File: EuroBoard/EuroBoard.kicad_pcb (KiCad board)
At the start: 2 copper layers, 100 x 100 mm, 21 parts, among them J1 SPI, SW1 RESET, SW2 BOOT, U1 AMS1117-3.3, U2 STM32G030CxT, Y1 NX2520 16MHz

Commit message: Started doing PCB
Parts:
- removed R3: R, Resistor_SMD:R_0805_2012Metric_Pad1.20x1.40mm_HandSolder
- removed SW2: BOOT, Button_Switch_SMD:SW_SPST_B3U-1000P-B
- added C10: 100n, Capacitor_SMD:C_0805_2012Metric_Pad1.18x1.45mm_HandSolder, F.Cu at (146.1, 48.3)
- added C11: 10u, Capacitor_SMD:C_0805_2012Metric_Pad1.18x1.45mm_HandSolder, F.Cu at (146.1, 50.8)
- added C9: 10u, Capacitor_SMD:C_0805_2012Metric_Pad1.18x1.45mm_HandSolder, F.Cu at (153.7, 50.8)
- added D2: 1n4148, Diode_SMD:D_SOD-123, F.Cu at (156.1, 79.2)
- added J2: I2C, Connector_PinSocket_2.54mm:PinSocket_1x03_P2.54mm_Vertical, F.Cu at (101.6, 78.7)
- added J3: UART, Connector_PinSocket_2.54mm:PinSocket_1x03_P2.54mm_Vertical, F.Cu at (101.6, 55.9)
- C3, C8: moved to B.Cu
- C4: value 4.7u -> 10u; moved to B.Cu
- SW1: footprint Button_Switch_SMD:SW_SPST_B3U-1000P-B -> Button_Switch_SMD:SW_SPST_B3S-1000
- moved C8 75.2 mm to (146.3, 64.0), turned to 180 degrees
- moved F1 72.9 mm to (156.5, 50.7), turned to 90 degrees
- moved C5 72.2 mm to (152.2, 45.7)
- moved U2 71.5 mm to (151.3, 63.9), turned to 45 degrees
- moved C4 68.6 mm to (151.4, 66.0)
- moved C3 68.2 mm to (151.4, 64.0)
- moved L1 66.9 mm to (147.1, 44.7), turned to -90 degrees
- moved C1 62.5 mm to (142.2, 67.9), turned to 180 degrees
- moved SW1 60.1 mm to (92.0, 41.0)
- moved U1 56.5 mm to (154.3, 40.6), turned to 0 degrees
- moved C6 55.0 mm to (148.2, 39.4), turned to 90 degrees
- moved C2 55.0 mm to (142.2, 74.7), turned to 180 degrees
- moved D1 53.6 mm to (142.2, 62.0), turned to 180 degrees
- moved C7 53.2 mm to (139.1, 71.1), turned to 90 degrees
- moved R1 52.9 mm to (145.2, 71.1), turned to 90 degrees
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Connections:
- net Net-(R2-Pad2) renamed /LED
- C2 pad 1: /RST -> Net-(C2-Pad1)
- C6 pad 1: +3.3V -> Net-(L1-Pad1)
- C8 pad 1: +3.3V -> /VREF
- F1 pad 2: Net-(F1-Pad2) -> Net-(C5-Pad1)
- L1 pad 1: Net-(F1-Pad2) -> Net-(L1-Pad1)
- L1 pad 2: Net-(C5-Pad1) -> +3.3V
- SW1 pad 2: /RST -> Net-(C2-Pad1)
- U1 pad 2: +3.3V -> Net-(L1-Pad1)
- U2 pad 10: /RST -> Net-(C2-Pad1)
- U2 pad 29: /SCL -> /TX_AUX
- U2 pad 32: /SDA -> /RX_AUX
- U2 pad 45: unconnected-(U2-Pad45) -> /SCL
- U2 pad 46: unconnected-(U2-Pad46) -> /SDA
- U2 pad 5: +3.3V -> /VREF
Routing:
- net /SCL: track 0.00 -> 32.2 mm
- net +3.3V: track 0.00 -> 30.8 mm, vias 0 -> 2
- net GND: track 0.00 -> 30.6 mm, vias 0 -> 1
- net Net-(L1-Pad1): track 0.00 -> 13.4 mm
- net Net-(C5-Pad1): track 0.00 -> 11.5 mm
- net Net-(C2-Pad1): track 0.00 -> 10.7 mm
- net /OSC_IN: track 0.00 -> 8.60 mm
- net +5V: track 0.00 -> 7.74 mm
- net Net-(C7-Pad1): track 0.00 -> 6.98 mm
- net /VREF: track 0.00 -> 5.62 mm, vias 0 -> 1
- net /OSC_OUT: track 0.00 -> 5.04 mm
- net /LED: track 0.00 -> 4.14 mm
- net -12V: track 0.00 -> 2.54 mm
- net +12V: track 0.00 -> 2.54 mm
- net Net-(D1-Pad2): track 0.00 -> 2.05 mm

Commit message: Board outline
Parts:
- added C12: 10u, Capacitor_SMD:C_0805_2012Metric_Pad1.18x1.45mm_HandSolder, B.Cu at (131.1, 38.1)
- added C13: 10u, Capacitor_SMD:C_0805_2012Metric_Pad1.18x1.45mm_HandSolder, B.Cu at (131.1, 40.6)
- added C14: 10u, Capacitor_SMD:C_0805_2012Metric_Pad1.18x1.45mm_HandSolder, B.Cu at (131.1, 43.2)
- added C15: 10u, Capacitor_SMD:C_0805_2012Metric_Pad1.18x1.45mm_HandSolder, B.Cu at (131.1, 45.7)
- added J4: Conn_01x05_Male, Connector_PinHeader_2.54mm:PinHeader_1x05_P2.54mm_Vertical, F.Cu at (134.6, 38.1)
- added SW2: SW_DIP_x04, Button_Switch_SMD:SW_DIP_SPSTx04_Slide_Omron_A6H-4101_W6.15mm_P1.27mm, F.Cu at (155.0, 61.0)
- C4: value 10u -> 4.7u; moved to F.Cu
- J1: value SPI -> GPIO; footprint Connector_PinHeader_2.54mm:PinHeader_1x04_P2.54mm_Vertical -> Connector_PinHeader_2.54mm:PinHeader_1x08_P2.54mm_Vertical
- J2: value I2C -> Conn_01x07_Male; footprint Connector_PinSocket_2.54mm:PinSocket_1x03_P2.54mm_Vertical -> Connector_PinHeader_2.54mm:PinHeader_1x07_P2.54mm_Vertical
- J3: value UART -> I2C; footprint Connector_PinSocket_2.54mm:PinSocket_1x03_P2.54mm_Vertical -> Connector_PinHeader_2.54mm:PinHeader_1x03_P2.54mm_Vertical
- moved J3 57.0 mm to (156.0, 73.0)
- moved SW1 50.5 mm to (142.5, 40.2)
- moved J2 48.0 mm to (127.0, 38.0), turned to 0 degrees
- moved J1 25.9 mm to (127.0, 63.5), turned to 0 degrees
- moved R2 17.9 mm to (144.3, 46.2)
- moved C4 17.9 mm to (133.9, 62.5), turned to 135 degrees
- moved C10 16.2 mm to (135.6, 60.7), turned to 135 degrees
- moved D1 15.9 mm to (140.2, 46.2), turned to 0 degrees
- moved C9 14.9 mm to (160.5, 37.5), turned to 0 degrees
- moved D2 14.2 mm to (143.3, 73.2), turned to 45 degrees
- moved F1 10.5 mm to (160.5, 41.0), turned to 180 degrees
- moved C3 8.91 mm to (142.5, 63.8)
- moved C6 8.05 mm to (151.5, 46.7), turned to 180 degrees
- moved U2 7.64 mm to (144.2, 61.1)
- moved C1 7.18 mm to (135.4, 65.5), turned to -135 degrees
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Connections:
- J1 pad 1: /SPI1_SCK -> Net-(J1-Pad1)
- J1 pad 2: /SPI1_MISO -> /SPI1_SCK
- J1 pad 3: /SPI1_MISO -> /TX_DEBUG
- J1 pad 4: GND -> /RX_DEBUG
- J2 pad 1: /SCL2 -> Net-(J2-Pad1)
- J2 pad 2: /SDA2 -> Net-(J2-Pad2)
- J2 pad 3: GND -> Net-(J2-Pad3)
- J3 pad 1: /TX_AUX -> /SCL2
- J3 pad 2: /RX_AUX -> /SDA2
- U2 pad 11: unconnected-(U2-Pad11) -> Net-(J1-Pad1)
- U2 pad 15: unconnected-(U2-Pad15) -> Net-(J1-Pad5)
- U2 pad 16: unconnected-(U2-Pad16) -> Net-(J1-Pad6)
- U2 pad 24: unconnected-(U2-Pad24) -> Net-(U2-Pad24)
- U2 pad 25: unconnected-(U2-Pad25) -> Net-(U2-Pad25)
- U2 pad 26: unconnected-(U2-Pad26) -> Net-(U2-Pad26)
- U2 pad 27: unconnected-(U2-Pad27) -> Net-(U2-Pad27)
- U2 pad 42: unconnected-(U2-Pad42) -> Net-(J2-Pad1)
- U2 pad 43: unconnected-(U2-Pad43) -> Net-(J2-Pad2)
- U2 pad 44: unconnected-(U2-Pad44) -> Net-(J2-Pad3)
- U2 pad 47: unconnected-(U2-Pad47) -> Net-(J2-Pad6)
- U2 pad 48: unconnected-(U2-Pad48) -> Net-(J2-Pad7)
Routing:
- net +3.3V: track 30.8 -> 132.9 mm
- net /TX_DEBUG: track 0.00 -> 80.4 mm, vias 0 -> 1
- net /RX_DEBUG: track 0.00 -> 75.5 mm, vias 0 -> 1
- net /SWCLK: track 0.00 -> 65.9 mm
- net /SWDIO: track 0.00 -> 62.6 mm, vias 0 -> 1
- net /RST: track 0.00 -> 57.4 mm, vias 0 -> 1
- net /SDA: track 0.00 -> 51.3 mm, vias 0 -> 1
- net +5V: track 7.74 -> 55.1 mm
- net /SPI1_MOSI: track 0.00 -> 45.2 mm, vias 0 -> 1
- net /SPI1_MISO: track 0.00 -> 41.6 mm, vias 0 -> 1
- net Net-(C2-Pad1): track 10.7 -> 49.4 mm, vias 0 -> 2
- net Net-(J1-Pad6): track 0.00 -> 37.9 mm, vias 0 -> 1
- net +12V: track 2.54 -> 39.0 mm
- net Net-(J1-Pad5): track 0.00 -> 33.8 mm, vias 0 -> 1
- net -12V: track 2.54 -> 36.0 mm
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- added copper zone on B.Cu, net GND
- added copper zone on F.Cu, net GND

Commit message: Board awaiting review
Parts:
- removed C10, C3: 100n, Capacitor_SMD:C_0805_2012Metric_Pad1.18x1.45mm_HandSolder
- added J10: PD1, TestPoint:TestPoint_Pad_1.0x1.0mm, F.Cu at (143.3, 50.5)
- added J11: PD2, TestPoint:TestPoint_Pad_1.0x1.0mm, F.Cu at (141.0, 50.5)
- added J12: PD3, TestPoint:TestPoint_Pad_1.0x1.0mm, F.Cu at (138.7, 50.5)
- added J5: RX, TestPoint:TestPoint_Pad_1.0x1.0mm, F.Cu at (148.5, 55.4)
- added J6: TX, TestPoint:TestPoint_Pad_1.0x1.0mm, F.Cu at (150.0, 56.9)
- added J7: GND, TestPoint:TestPoint_Pad_1.0x1.0mm, F.Cu at (145.3, 50.5)
- added REF**: ProtoArea, MEMS_Custom:ProtoArea, F.Cu at (78.0, 37.0)
- L1: footprint Inductor_SMD:L_0805_2012Metric -> Inductor_SMD:L_0805_2012Metric_Pad1.15x1.40mm_HandSolder
- moved SW2 4.13 mm to (155.4, 56.9), turned to 90 degrees
- moved J3 2.93 mm to (156.5, 70.1)
- moved C4 1.21 mm to (133.6, 63.7), turned to -135 degrees
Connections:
- U2 pad 19: unconnected-(U2-Pad19) -> /TRG
- U2 pad 20: unconnected-(U2-Pad20) -> /RDY
- U2 pad 39: unconnected-(U2-Pad39) -> Net-(U2-Pad39)
- U2 pad 40: unconnected-(U2-Pad40) -> Net-(U2-Pad40)
- U2 pad 41: unconnected-(U2-Pad41) -> Net-(U2-Pad41)
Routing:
- net /RDY: track 0.00 -> 38.3 mm, vias 0 -> 1
- net /TRG: track 0.00 -> 36.7 mm, vias 0 -> 1
- net +3.3V: track 132.9 -> 145.6 mm
- net +5V: track 55.1 -> 67.5 mm, vias 0 -> 1
- net /SWDIO: track 62.6 -> 73.9 mm
- net /SWCLK: track 65.9 -> 75.9 mm
- net /SCL: track 50.1 -> 59.6 mm
- net Net-(U2-Pad41): track 0.00 -> 8.37 mm
- net /RX_DEBUG: track 75.5 -> 83.6 mm
- net Net-(SW2-Pad4): track 3.14 -> 11.2 mm
- net /TX_DEBUG: track 80.4 -> 88.2 mm
- net Net-(U2-Pad40): track 0.00 -> 7.64 mm
- net Net-(U2-Pad39): track 0.00 -> 7.33 mm
- net /SDA: track 51.3 -> 58.4 mm
- net -12V: track 36.0 -> 42.8 mm
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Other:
- board text added: "-12V"
- board text added: "12V"
- board text added: "3.3V"
- board text added: "5V"
- board text added: "EuroMeasure Evaluation Module v1.0"
- board text added: "GND"
- board text added: "Michał Zychla 2023"
- board text added: "SCL"
- board text added: "SDA"

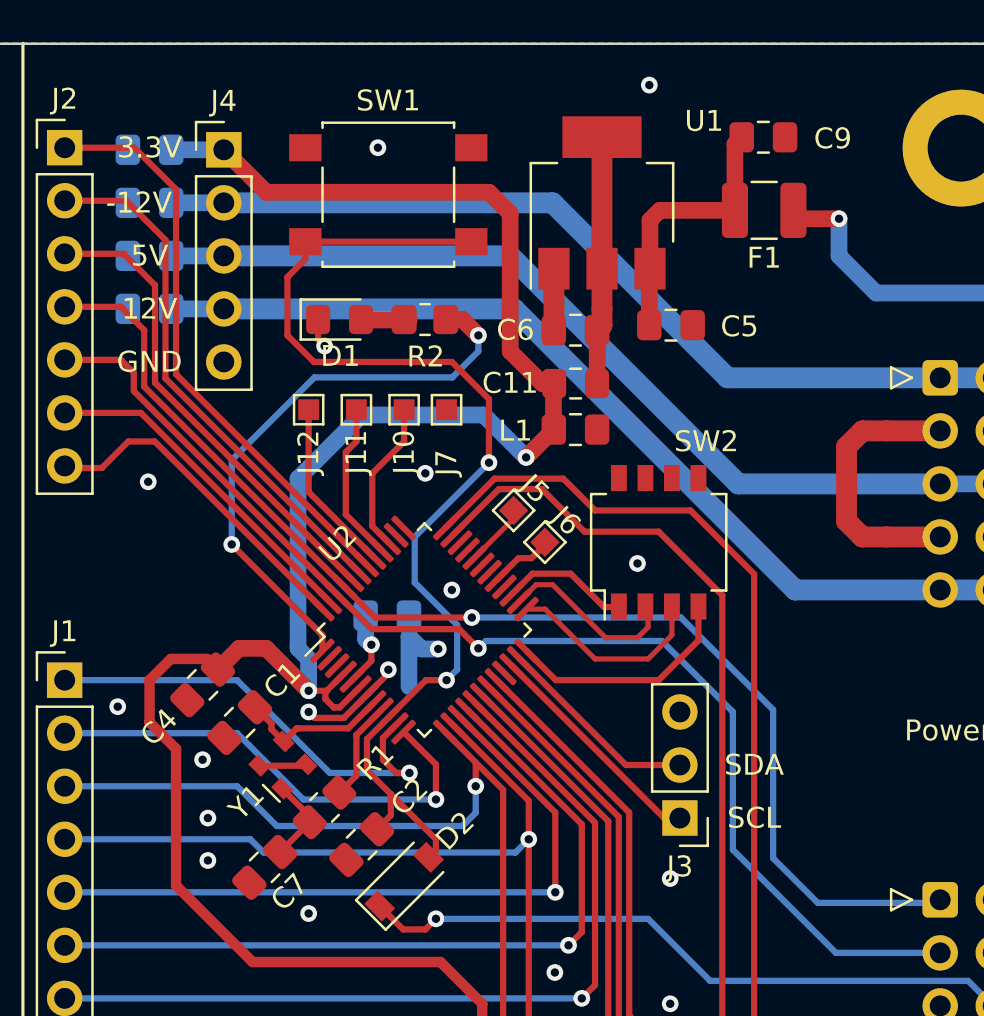
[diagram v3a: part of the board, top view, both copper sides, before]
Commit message: Removed unnecessary caps
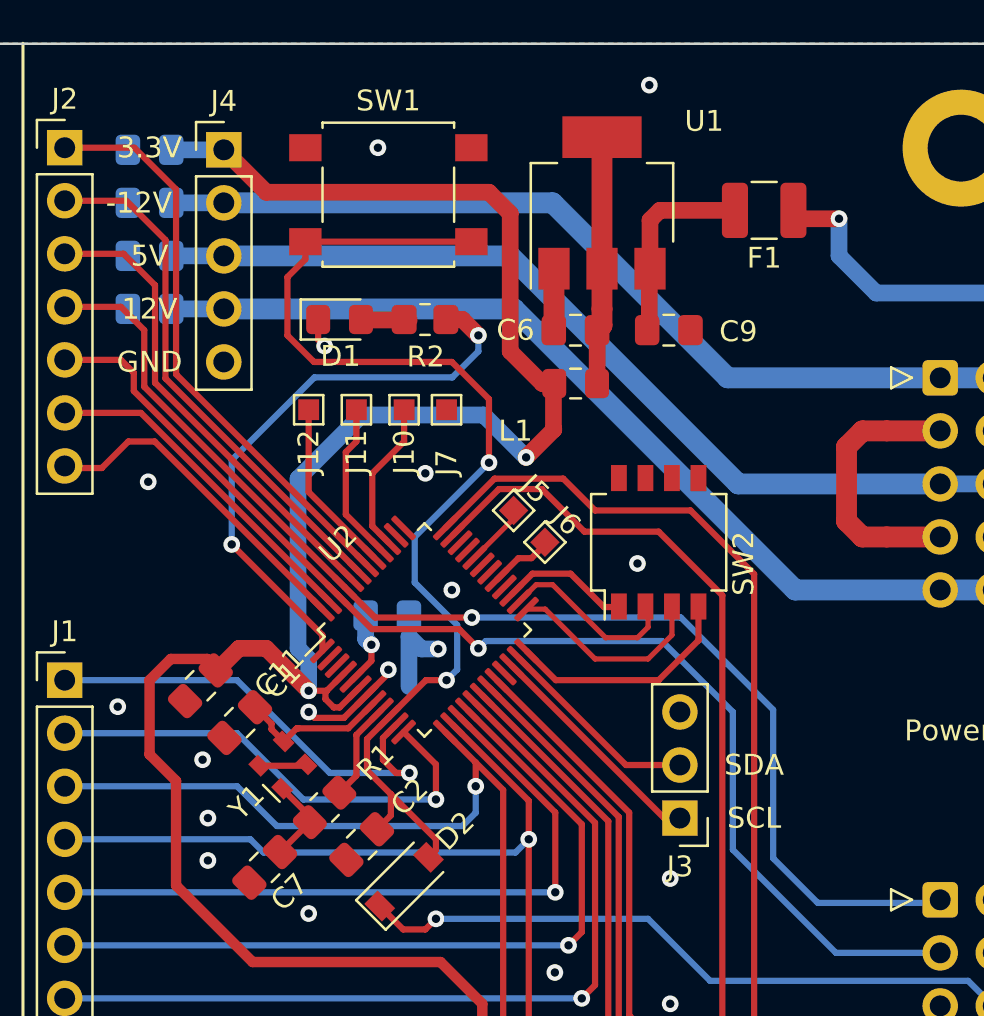
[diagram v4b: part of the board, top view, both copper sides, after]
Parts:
- removed C4: 4.7u, Capacitor_SMD:C_0805_2012Metric_Pad1.18x1.45mm_HandSolder
- removed C5: 1u, Capacitor_SMD:C_0805_2012Metric_Pad1.18x1.45mm_HandSolder
- moved C11 21.8 mm to (133.5, 63.8), turned to -135 degrees
- moved C9 10.3 mm to (155.9, 46.7)
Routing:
- net Net-(C5-Pad1): track 12.9 -> 9.31 mm

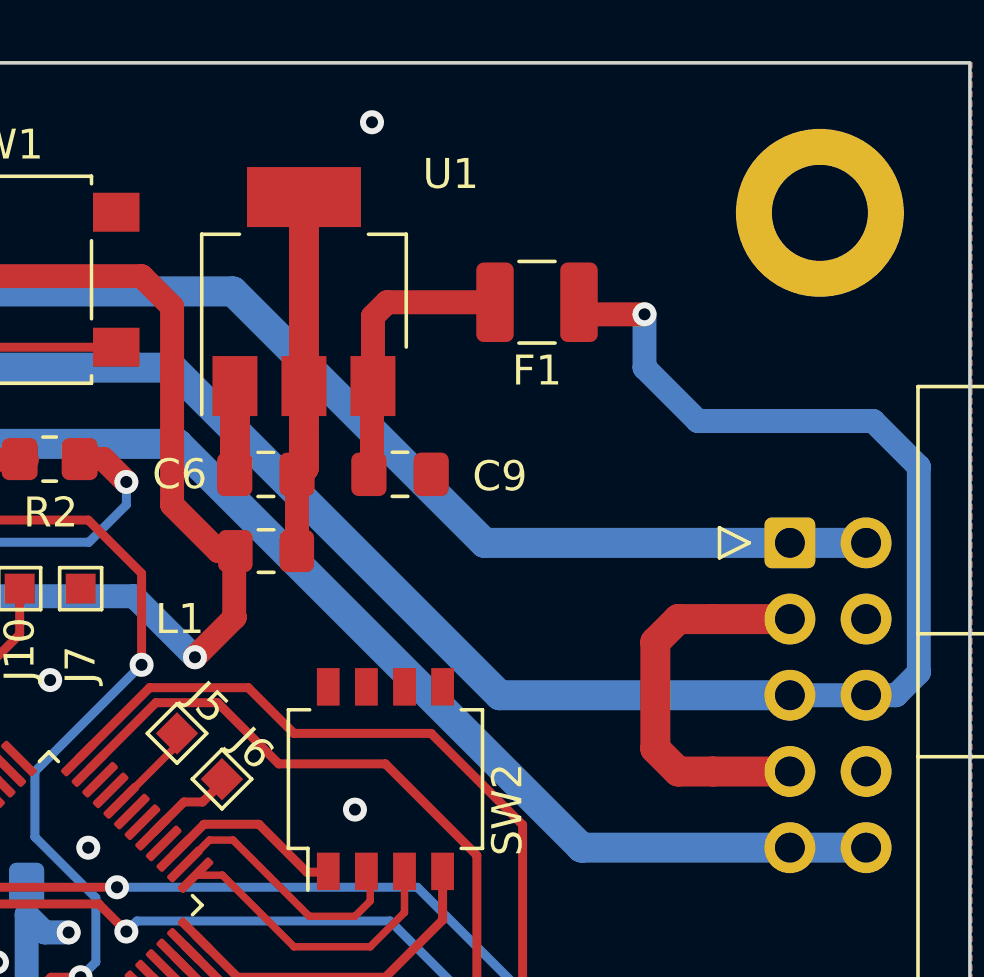
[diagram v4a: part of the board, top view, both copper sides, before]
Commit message: Added alectrolytic capacitors
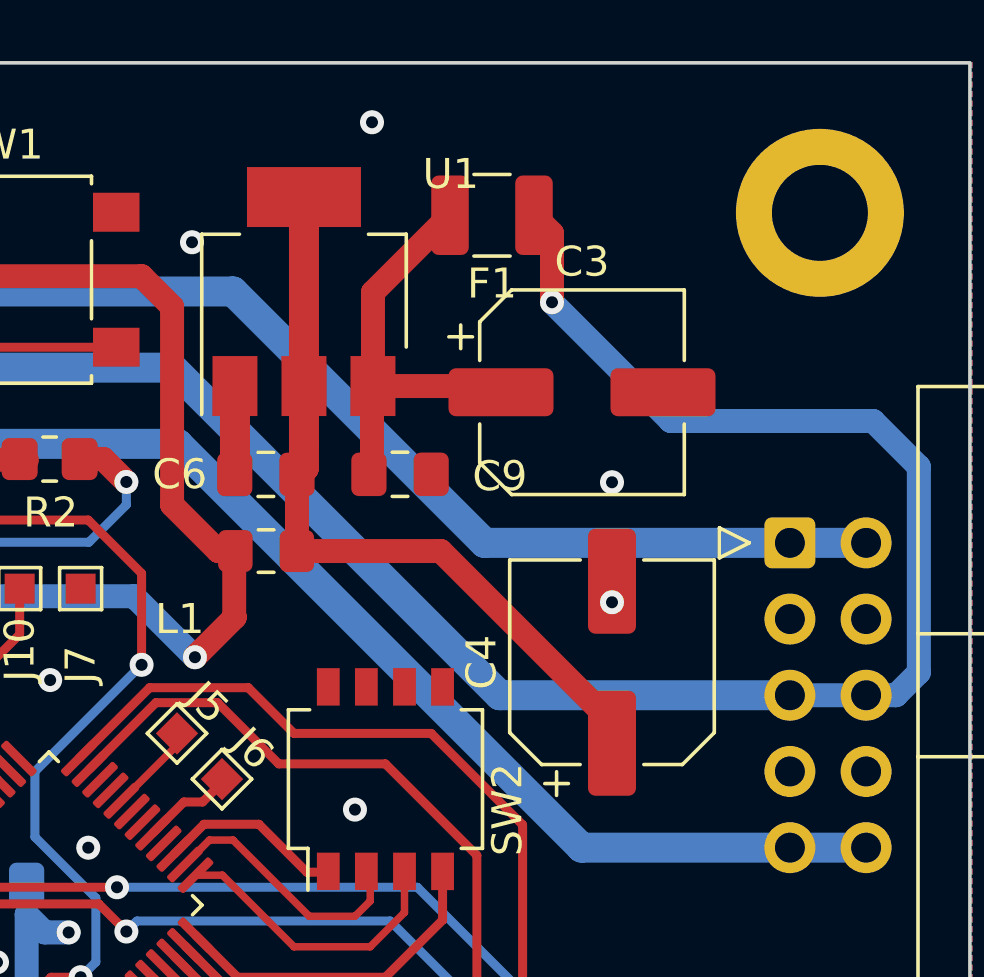
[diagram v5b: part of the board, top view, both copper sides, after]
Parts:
- added C3: 220u, Capacitor_SMD:CP_Elec_6.3x7.7, F.Cu at (162.0, 44.0)
- added C4: 220u, Capacitor_SMD:CP_Elec_6.3x7.7, F.Cu at (163.0, 53.0)
- C6: value 4.7u -> 10u
- moved F1 3.26 mm to (159.0, 38.1)
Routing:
- net Net-(C6-Pad1): track 12.3 -> 25.9 mm
- net GND: track 29.2 -> 16.1 mm, vias 21 -> 24
- net Net-(C9-Pad1): track 9.31 -> 13.8 mm
- net +5V: track 67.5 -> 70.5 mm

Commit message: Connected free bus lines to GPIO
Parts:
- moved C8 3.54 mm to (140.0, 63.0), turned to -90 degrees
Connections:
- B1 pad 15: unconnected-(B1-Pad15) -> /GP2
- B1 pad 17: unconnected-(B1-Pad17) -> /GP0
- B1 pad 18: unconnected-(B1-Pad18) -> /GP1
- U2 pad 21: unconnected-(U2-Pad21) -> /GP2
- U2 pad 33: unconnected-(U2-Pad33) -> /GP0
- U2 pad 34: unconnected-(U2-Pad34) -> /GP1
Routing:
- net /GP0: track 0.00 -> 41.6 mm, vias 0 -> 2
- net /GP1: track 0.00 -> 41.1 mm, vias 0 -> 2
- net /GP2: track 0.00 -> 28.0 mm, vias 0 -> 1
- net GND: track 16.1 -> 12.1 mm, vias 24 -> 25
- net +3.3V: track 145.6 -> 141.7 mm
- net /RST: track 63.7 -> 66.2 mm
- net Net-(C2-Pad1): track 53.8 -> 52.0 mm
